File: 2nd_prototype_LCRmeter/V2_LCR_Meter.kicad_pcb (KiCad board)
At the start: 6 copper layers, 99.9 x 99.9 mm, 202 parts, among them J1 Conn_Coaxial, J2 Conn_Coaxial, J3 Conn_Coaxial, J4 Conn_Coaxial, J5 USB_C_Receptacle_USB2.0_16P, J6 IDC 2x5, J7 Display OLED, K1 Relay_DPDT, Q1 NX3008NBK, Q2 NX3008NBK, Q3 NX3008NBK, SW1 SW_SPST, SW2 SW_SPST, SW3 SW_SPST, U1 AD9837, U10 ESP32-S2-SOLO-N4, U12 TL074, U13 MCP4561-502E_MS, U14 CD74HC4052, U16 CD74HC4052, U17 INA823, U18 CD74HC4052, U19 74LVC1G02, U2 TLV9154, U20 CD74HC4052, U21 INA823, U23 CD74HC4052, U3 ADS1115IDGS, U4 LM393, U5 TLV9154, U7 TDC7200PWR, U8 LM27762, U9 HT75xx-1-SOT89, X1 SG-210STF, X2 SG-210STF

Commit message: work on layout proto2
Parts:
- removed  : TestPoint_THTPad_D2.5mm_Drill1.2mm, TestPoint:TestPoint_THTPad_D2.5mm_Drill1.2mm (x8)
- removed  : G***, kibuzzard-678FA556 (x2)
- removed  : G***, kibuzzard-678FA586 (x2)
- removed  : G***, kibuzzard-678FA580 (x2)
- removed  : G***, kibuzzard-678FA578 (x2)
- removed ? (x4): MountingHole_2.2mm_M2_DIN965_Pad, MountingHole:MountingHole_2.2mm_M2_DIN965_Pad
- removed D19, D21, D22, D23: WS2812B, LED_SMD:LED_WS2812B_PLCC4_5.0x5.0mm_P3.2mm
- removed D20: LED, LED_SMD:LED_miniPLCC_2315
- removed J5: USB_C_Receptacle_USB2.0_16P, Connector_USB:USB_C_Receptacle_GCT_USB4105-xx-A_16P_TopMnt_Horizontal
- removed Q2, Q3: NX3008NBK, Package_TO_SOT_SMD:SOT-323_SC-70_Handsoldering
- removed SW2, SW3: SW_SPST, Snapeda:SW-SMD_L6.1-W3.7-LS7.9
- removed U21: INA823, Package_SO:SOIC-8_3.9x4.9mm_P1.27mm
- removed U22: ~, Snapeda:AD9833_Module
- removed U23: CD74HC4052, Package_SO:TSSOP-16_4.4x5mm_P0.65mm
- removed X2: SG-210STF, Oscillator:Oscillator_SMD_SeikoEpson_SG210-4Pin_2.5x2.0mm
- removed kibuzzard-678FC38E: G***, kibuzzard-678FC38E
- removed kibuzzard-678FC3F7: G***, kibuzzard-678FC3F7
- removed kibuzzard-678FC3FC: G***, kibuzzard-678FC3FC
- removed kibuzzard-678FC401: G***, kibuzzard-678FC401
- removed kibuzzard-6790BC5C (x2): G***, kibuzzard-6790BC5C
- removed kibuzzard-6790BC71 (x2): G***, kibuzzard-6790BC71
- removed kibuzzard-6790BC83 (x2): G***, kibuzzard-6790BC83
- removed kibuzzard-6790BC8C (x2): G***, kibuzzard-6790BC8C
- removed kibuzzard-6790BCCF: G***, kibuzzard-6790BCCF
- removed kibuzzard-6790BCE4: G***, kibuzzard-6790BCE4
- removed kibuzzard-6790BCFE: G***, kibuzzard-6790BCFE
- removed kibuzzard-6790BDCA: G***, kibuzzard-6790BDCA
- removed kibuzzard-6790BDD8: G***, kibuzzard-6790BDD8
- removed kibuzzard-6790BDEA: G***, kibuzzard-6790BDEA
- removed kibuzzard-6790BDF0: G***, kibuzzard-6790BDF0
- removed kibuzzard-67960D2E: G***, kibuzzard-67960D2E
- removed kibuzzard-67C21963: G***, kibuzzard-67C21963
- added C24: 1u, Capacitor_SMD:C_0603_1608Metric_Pad1.08x0.95mm_HandSolder, F.Cu at (89.8, 41.0)
- added C52: 1u, Capacitor_SMD:C_0603_1608Metric_Pad1.08x0.95mm_HandSolder, F.Cu at (72.9, 91.9)
- added C53: 1u, Capacitor_SMD:C_0603_1608Metric_Pad1.08x0.95mm_HandSolder, B.Cu at (252.5, 80.8)
- added C54: 100n, Capacitor_SMD:C_0603_1608Metric_Pad1.08x0.95mm_HandSolder, B.Cu at (251.1, 76.4)
- added C55: 1u, Capacitor_SMD:C_0603_1608Metric_Pad1.08x0.95mm_HandSolder, B.Cu at (249.5, 69.7)
- added C56: 100n, Capacitor_SMD:C_0603_1608Metric_Pad1.08x0.95mm_HandSolder, B.Cu at (269.8, 84.2)
- added J8: Conn_Coaxial, Snapeda:BNC_Gold, F.Cu at (257.9, 118.5)
- added J9: Conn_Coaxial, Snapeda:BNC_Gold, F.Cu at (191.9, 118.5)
- added JP5: SolderJumper_2_Open, Jumper:SolderJumper-2_P1.3mm_Open_RoundedPad1.0x1.5mm, F.Cu at (264.4, 73.3)
- added JP6: SolderJumper_2_Open, Jumper:SolderJumper-2_P1.3mm_Open_RoundedPad1.0x1.5mm, F.Cu at (264.5, 65.6)
- added R20: 100R, Resistor_SMD:R_0603_1608Metric_Pad0.98x0.95mm_HandSolder, F.Cu at (102.8, 28.4)
- added R50: 10k, Resistor_SMD:R_0603_1608Metric_Pad0.98x0.95mm_HandSolder, F.Cu at (111.5, 38.5)
- added R51: 10k, Resistor_SMD:R_0603_1608Metric_Pad0.98x0.95mm_HandSolder, F.Cu at (111.5, 41.0)
- added R52: 10k, Resistor_SMD:R_0603_1608Metric_Pad0.98x0.95mm_HandSolder, F.Cu at (111.5, 43.5)
- added R53: 10k, Resistor_SMD:R_0603_1608Metric_Pad0.98x0.95mm_HandSolder, F.Cu at (111.5, 46.0)
- added R54: 10k, Resistor_SMD:R_0603_1608Metric_Pad0.98x0.95mm_HandSolder, F.Cu at (111.5, 48.5)
- added R55: 10k, Resistor_SMD:R_0603_1608Metric_Pad0.98x0.95mm_HandSolder, F.Cu at (111.5, 51.0)
- added R56: 10k, Resistor_SMD:R_0603_1608Metric_Pad0.98x0.95mm_HandSolder, B.Cu at (253.6, 73.3)
- added R57: 33k, Resistor_SMD:R_0603_1608Metric_Pad0.98x0.95mm_HandSolder, B.Cu at (257.0, 73.3)
- added R58: 100k, Resistor_SMD:R_0603_1608Metric_Pad0.98x0.95mm_HandSolder, B.Cu at (251.1, 73.1)
- added R59: 100k, Resistor_SMD:R_0603_1608Metric_Pad0.98x0.95mm_HandSolder, B.Cu at (251.1, 69.7)
- added R60: 10k, Resistor_SMD:R_0603_1608Metric_Pad0.98x0.95mm_HandSolder, B.Cu at (247.9, 69.7)
- added R61: 10k, Resistor_SMD:R_0603_1608Metric_Pad0.98x0.95mm_HandSolder, B.Cu at (247.9, 73.1)
- added R62: 10k, Resistor_SMD:R_0603_1608Metric_Pad0.98x0.95mm_HandSolder, B.Cu at (249.5, 73.1)
- added R63: 1k, Resistor_SMD:R_0603_1608Metric_Pad0.98x0.95mm_HandSolder, F.Cu at (205.9, 38.5)
- added R64: 10k, Resistor_SMD:R_0603_1608Metric_Pad0.98x0.95mm_HandSolder, F.Cu at (239.2, 44.8)
- added R65: 5k1, Resistor_SMD:R_0603_1608Metric_Pad0.98x0.95mm_HandSolder, F.Cu at (218.1, 30.4)
- added R66: 5k1, Resistor_SMD:R_0603_1608Metric_Pad0.98x0.95mm_HandSolder, F.Cu at (218.1, 27.0)
- added TP1: TestPoint, Connector_Pin:Pin_D1.0mm_L10.0mm, F.Cu at (80.5, 62.2)
- added TP10: TestPoint, Connector_Pin:Pin_D1.0mm_L10.0mm, F.Cu at (84.6, 78.4)
- added TP11: TestPoint, Connector_Pin:Pin_D1.0mm_L10.0mm, F.Cu at (272.0, 34.0)
- added TP12: TestPoint, Connector_Pin:Pin_D1.0mm_L10.0mm, F.Cu at (272.0, 38.0)
- added TP13: TestPoint, Connector_Pin:Pin_D1.0mm_L10.0mm, F.Cu at (272.0, 42.0)
- added TP14: TestPoint, Connector_Pin:Pin_D1.0mm_L10.0mm, F.Cu at (272.0, 46.0)
- added TP15: TestPoint, Connector_Pin:Pin_D1.0mm_L10.0mm, F.Cu at (229.0, 68.6)
- added TP16: TestPoint, Connector_Pin:Pin_D1.0mm_L10.0mm, F.Cu at (229.0, 72.7)
- added TP17: TestPoint, Connector_Pin:Pin_D1.0mm_L10.0mm, F.Cu at (229.0, 76.7)
- added TP18: TestPoint, Connector_Pin:Pin_D1.0mm_L10.0mm, F.Cu at (229.0, 80.8)
- added TP19: TestPoint, Connector_Pin:Pin_D1.0mm_L10.0mm, F.Cu at (229.0, 84.8)
- added TP2: TestPoint, Connector_Pin:Pin_D1.0mm_L10.0mm, F.Cu at (80.5, 66.2)
- added TP20: TestPoint, Connector_Pin:Pin_D1.0mm_L10.0mm, F.Cu at (270.1, 90.8)
- added TP21: TestPoint, Connector_Pin:Pin_D1.0mm_L10.0mm, F.Cu at (268.8, 104.1)
- added TP3: TestPoint, Connector_Pin:Pin_D1.0mm_L10.0mm, F.Cu at (80.5, 70.3)
- added TP4: TestPoint, Connector_Pin:Pin_D1.0mm_L10.0mm, F.Cu at (80.5, 74.3)
- added TP5: TestPoint, Connector_Pin:Pin_D1.0mm_L10.0mm, F.Cu at (80.5, 78.4)
- added TP6: TestPoint, Connector_Pin:Pin_D1.0mm_L10.0mm, F.Cu at (84.6, 62.2)
- added TP7: TestPoint, Connector_Pin:Pin_D1.0mm_L10.0mm, F.Cu at (84.6, 66.2)
- added TP8: TestPoint, Connector_Pin:Pin_D1.0mm_L10.0mm, F.Cu at (84.6, 70.3)
- added TP9: TestPoint, Connector_Pin:Pin_D1.0mm_L10.0mm, F.Cu at (84.6, 74.3)
- added U11: CD74HC4052, Package_SO:TSSOP-16_4.4x5mm_P0.65mm, F.Cu at (83.3, 43.7)
- added U15: REF3033, Package_TO_SOT_SMD:SOT-23, F.Cu at (116.2, 38.2)
- added U6: INA823, Package_SO:SOIC-8_3.9x4.9mm_P1.27mm, F.Cu at (91.8, 69.8)
- added Y1: 8MHz, Crystal:Crystal_HC49-U_Vertical, F.Cu at (182.5, 40.6)
- added kibuzzard-699D9FD2: G***, kibuzzard-699D9FD2, F.Cu at (236.0, 40.0)
- added kibuzzard-699DA048: G***, kibuzzard-699DA048, F.Cu at (267.0, 34.0)
- added kibuzzard-699DA05C: G***, kibuzzard-699DA05C, F.Cu at (267.0, 38.0)
- added kibuzzard-699DA06A: G***, kibuzzard-699DA06A, F.Cu at (224.0, 72.6)
- added kibuzzard-699DA06A: G***, kibuzzard-699DA06A, F.Cu at (267.0, 42.0)
- added kibuzzard-699DA06A: G***, kibuzzard-699DA06A, F.Cu at (224.0, 68.6)
- added kibuzzard-699DA06A: G***, kibuzzard-699DA06A, F.Cu at (224.0, 76.6)
- added kibuzzard-699DA06A: G***, kibuzzard-699DA06A, F.Cu at (224.0, 84.6)
- added kibuzzard-699DA06A: G***, kibuzzard-699DA06A, F.Cu at (224.0, 80.6)
- added kibuzzard-699DA06F: G***, kibuzzard-699DA06F, F.Cu at (267.0, 46.0)
- added kibuzzard-699DB946: G***, kibuzzard-699DB946, F.Cu at (266.2, 91.7)
- C1, C2: value 4.7u -> 20p; footprint Capacitor_SMD:C_0805_2012Metric_Pad1.18x1.45mm_HandSolder -> Capacitor_SMD:C_0603_1608Metric_Pad1.08x0.95mm_HandSolder; moved to F.Cu
- C10: footprint Capacitor_SMD:C_0603_1608Metric_Pad1.08x0.95mm_HandSolder -> Resistor_SMD:R_0603_1608Metric_Pad0.98x0.95mm_HandSolder; moved to F.Cu
- C11, C12: value 470u -> 100n; footprint Capacitor_THT:CP_Radial_D8.0mm_P3.80mm -> Capacitor_SMD:C_0603_1608Metric_Pad1.08x0.95mm_HandSolder
- C13, C15: value 1u -> 4.7u; footprint Capacitor_SMD:C_0603_1608Metric_Pad1.08x0.95mm_HandSolder -> Capacitor_SMD:C_0603_1608Metric; moved to F.Cu
- C14, C19, C4, C5: value 100n -> 1u; moved to F.Cu
- C16: value 10n -> 4.7u; footprint Capacitor_SMD:C_0603_1608Metric_Pad1.08x0.95mm_HandSolder -> Capacitor_SMD:C_0603_1608Metric; moved to F.Cu
- C17: value 1u -> 10n
- C18, C7: value 1u -> 470u; footprint Capacitor_SMD:C_0603_1608Metric_Pad1.08x0.95mm_HandSolder -> Capacitor_THT:CP_Radial_D8.0mm_P3.80mm; moved to F.Cu
- C20, C21, C22, C23, C25, C26, C27, C29, C30, C31, C35, C36, C37, C38, C41, C43, C47, C49, R15, R18, R2, R35, R5, R6, R8: moved to F.Cu
- C28, C32, C33, C34, C44, C45, C46: value 1u -> 330n; moved to F.Cu
- C3: footprint Resistor_SMD:R_0603_1608Metric_Pad0.98x0.95mm_HandSolder -> Capacitor_SMD:C_0603_1608Metric_Pad1.08x0.95mm_HandSolder; moved to F.Cu
- C39, C40, C42: value 330n -> 1u; moved to F.Cu
- C48, C50: value 1u -> 100n; moved to F.Cu
- C51: value 470u -> 1u; footprint Capacitor_THT:CP_Radial_D8.0mm_P3.80mm -> Capacitor_SMD:C_0603_1608Metric_Pad1.08x0.95mm_HandSolder
- C6: value 4.7u -> 1u; footprint Capacitor_SMD:C_0805_2012Metric_Pad1.18x1.45mm_HandSolder -> Capacitor_SMD:C_0603_1608Metric_Pad1.08x0.95mm_HandSolder; moved to F.Cu
- C8, C9: footprint Capacitor_SMD:C_0805_2012Metric_Pad1.18x1.45mm_HandSolder -> Capacitor_SMD:C_0603_1608Metric; moved to F.Cu
- D14: value LED -> D_Schottky; footprint LED_SMD:LED_miniPLCC_2315 -> Diode_SMD:D_MiniMELF
- D15, D17: value LED -> WS2812B; footprint LED_SMD:LED_miniPLCC_2315 -> LED_SMD:LED_WS2812B_PLCC4_5.0x5.0mm_P3.2mm
- D18: footprint LED_SMD:LED_miniPLCC_2315 -> LED_SMD:LED_miniPLCC_2315_Handsoldering
- D2: value D_Schottky -> LED; footprint Diode_SMD:D_MiniMELF -> LED_SMD:LED_miniPLCC_2315
- D3, D4, D5, D6: value SS14 -> LED; footprint Diode_SMD:D_SMA -> LED_SMD:LED_miniPLCC_2315
- J1: value Conn_Coaxial -> ST-Link; footprint Connector_Coaxial:BNC_Amphenol_B6252HB-NPP3G-50_Horizontal -> Connector_PinHeader_2.54mm:PinHeader_1x04_P2.54mm_Vertical_SMD_Pin1Left
- J2: value Conn_Coaxial -> Display OLED; footprint Connector_Coaxial:BNC_Amphenol_B6252HB-NPP3G-50_Horizontal -> Connector:FanPinHeader_1x04_P2.54mm_Vertical
- J3: value Conn_Coaxial -> IDC 2x5; footprint Connector_Coaxial:BNC_Amphenol_B6252HB-NPP3G-50_Horizontal -> Connector_IDC:IDC-Header_2x05_P2.54mm_Vertical
- J4: value Conn_Coaxial -> USB_C_Receptacle_USB2.0_16P; footprint Connector_Coaxial:BNC_Amphenol_B6252HB-NPP3G-50_Horizontal -> Connector_USB:USB_C_Receptacle_GCT_USB4105-xx-A_16P_TopMnt_Horizontal
- J6: value IDC 2x5 -> Conn_Coaxial; footprint Connector_IDC:IDC-Header_2x05_P2.54mm_Vertical -> Snapeda:BNC_Gold
- J7: value Display OLED -> Conn_Coaxial; footprint Connector:FanPinHeader_1x04_P2.54mm_Vertical -> Snapeda:BNC_Gold
- JP1: value SolderJumper_3_Open -> Jumper_3_Open; footprint Jumper:SolderJumper-3_P1.3mm_Open_RoundedPad1.0x1.5mm -> Connector_PinHeader_2.54mm:PinHeader_1x03_P2.54mm_Vertical_SMD_Pin1Left
- JP4: footprint Jumper:SolderJumper-2_P1.3mm_Open_TrianglePad1.0x1.5mm -> Jumper:SolderJumper-2_P1.3mm_Open_RoundedPad1.0x1.5mm
- K1: footprint Relay_THT:Relay_CIT-J104D -> Relay_THT:Relay_DPDT_Finder_30.22
- R1, R19, R22, R42, R45, R46, R47, R48, R49: value 1k -> 10k; moved to F.Cu
- R10: value 10k -> 1k5; moved to F.Cu
- R11: value 33k -> 1k5; moved to F.Cu
- R12: value 10k -> 4k7; moved to F.Cu
- R13, R37, R38: value 10k -> 1k; moved to F.Cu
- R14: value 10k -> 200k; moved to F.Cu
- R16: value 100R -> 22k; moved to F.Cu
- R17, R24, R27: value 100k -> 10k; moved to F.Cu
- R21: value 100R -> 1k; moved to F.Cu
- R23, R36: value 10k -> 100k; moved to F.Cu
- R25, R29, R30, R31: value 0R -> 10k; moved to F.Cu
- R26, R32: value 200k -> 10k; moved to F.Cu
- R28: value 22k -> 10k; moved to F.Cu
- R3, R4: value 1k5 -> 10k; moved to F.Cu
- R33: value 100k -> 100R; moved to F.Cu
- R34: value 22k -> 1k; moved to F.Cu
- R39: value 100k -> 200k; moved to F.Cu
- R40: value 1k -> 100k; moved to F.Cu
- R41: value 100k -> 22k; moved to F.Cu
- R43, R44: value 4k7 -> 10k; moved to F.Cu
- R7: value 1k -> 1k5; moved to F.Cu
- R9: value 100k -> 4k7; moved to F.Cu
- U1: value AD9837 -> STM32F103C8Tx; footprint Snapeda:AD9837_AD9837 -> Package_QFP:LQFP-48_7x7mm_P0.5mm
- U10: value ESP32-S2-SOLO-N4 -> TL072; footprint Snapeda:ESP32-S2-SOLO-N4_XCVR_ESP32-S2-SOLO-N4 -> Package_SO:SOIC-8_3.9x4.9mm_P1.27mm
- U12: value TL074 -> INA823; footprint Package_SO:TSSOP-14_4.4x5mm_P0.65mm -> Package_SO:SOIC-8_3.9x4.9mm_P1.27mm
- U13: value MCP4561-502E_MS -> CD74HC4052; footprint Snapeda:MCP4561-502E_MS_SOP65P490X110-8N -> Package_SO:TSSOP-16_4.4x5mm_P0.65mm
- U16: value CD74HC4052 -> 74LVC1G02; footprint Package_SO:TSSOP-16_4.4x5mm_P0.65mm -> Package_TO_SOT_SMD:SOT-23-5_HandSoldering
- U17: value INA823 -> ~; footprint Package_SO:SOIC-8_3.9x4.9mm_P1.27mm -> Snapeda:AD9833_Module
- U18: value CD74HC4052 -> TL074; footprint Package_SO:TSSOP-16_4.4x5mm_P0.65mm -> Package_SO:TSSOP-14_4.4x5mm_P0.65mm
- U19: value 74LVC1G02 -> MCP4561-502E_MS; footprint Package_TO_SOT_SMD:SOT-23-5_HandSoldering -> Package_SO:MSOP-8_3x3mm_P0.65mm
- U2: value TLV9154 -> LM27762; footprint Package_SO:SOIC-14_3.9x8.7mm_P1.27mm -> Package_SON:WSON-12-1EP_3x2mm_P0.5mm_EP1x2.65_ThermalVias
- U20: value CD74HC4052 -> AD9837; footprint Package_SO:TSSOP-16_4.4x5mm_P0.65mm -> Package_CSP:LFCSP-WD-10-1EP_3x3mm_P0.5mm_EP1.64x2.38mm
- U3: value ADS1115IDGS -> HT75xx-1-SOT89; footprint Package_SO:TSSOP-10_3x3mm_P0.5mm -> Package_TO_SOT_SMD:SOT-89-3_Handsoldering
- U4: value LM393 -> OPA2192
- U5: value TLV9154 -> CD74HC4052; footprint Package_SO:SOIC-14_3.9x8.7mm_P1.27mm -> Package_SO:TSSOP-16_4.4x5mm_P0.65mm
- U7: value TDC7200PWR -> TL074; footprint Snapeda:TDC7200PWR_SOP65P640X120-14N -> Package_SO:TSSOP-14_4.4x5mm_P0.65mm
- U8: value LM27762 -> CD74HC4052; footprint Package_SON:WSON-12-1EP_3x2mm_P0.5mm_EP1x2.65_ThermalVias -> Package_SO:TSSOP-16_4.4x5mm_P0.65mm
- U9: value HT75xx-1-SOT89 -> TL074; footprint Package_TO_SOT_SMD:SOT-89-3_Handsoldering -> Package_SO:TSSOP-14_4.4x5mm_P0.65mm
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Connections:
- C1 pad 1: +5V_USB -> Net-(U1-PD0)
- C10 pad 1: GND -> Net-(U2-C+)
- C10 pad 2: +3V3 -> Net-(U2-C-)
- C12 pad 1: -5V -> +3V3
- C13 pad 1: GND -> Net-(U2-CP)
- C13 pad 2: +3V3 -> GND
- C14 pad 1: GND -> +3V3
- C14 pad 2: Net-(U1-CAP/2.5V) -> GND
- C15 pad 1: GND -> +5V_USB
- C15 pad 2: Net-(U1-CAP/2.5V) -> GND
- C16 pad 1: Net-(U1-COMP) -> +5V
- C16 pad 2: +3V3 -> GND
- C17 pad 1: GND -> +3V3
- C17 pad 2: +5V -> Net-(U20-COMP)
- C18 pad 1: GND -> -5V
- C18 pad 2: -5V -> GND
- C19 pad 1: Net-(U12B-+) -> GND
- C19 pad 2: Net-(U13-P0W) -> +5V
- C2 pad 1: +5V_USB -> Net-(U1-PD1)
- C20 pad 2: +3V3 -> -5V
- C21 pad 2: Net-(U12D-+) -> -5V
- C23 pad 2: +5V -> -5V
- C27 pad 2: +5V -> -5V
- C28 pad 1: GND -> Net-(C28-Pad1)
- C28 pad 2: -5V -> Net-(C28-Pad2)
- C3 pad 1: Net-(U8-C+) -> GND
- C3 pad 2: Net-(U8-C-) -> +3V3
- C32 pad 1: GND -> Net-(U7C-+)
- C32 pad 2: -5V -> Net-(C28-Pad1)
- C33 pad 1: GND -> Net-(U7A-+)
- C33 pad 2: -5V -> GND
- C34 pad 1: GND -> /Analog frontend/V_LowPass
- C34 pad 2: -5V -> Net-(C34-Pad2)
- C35 pad 2: -5V -> +5V
- C36 pad 2: +5V -> -5V
- C37 pad 2: +5V -> -5V
- C38 pad 2: -5V -> +5V
- C39 pad 1: V_Mean -> GND
- C39 pad 2: Net-(C39-Pad2) -> -5V
- C4 pad 1: +5V_USB -> GND
- C4 pad 2: GND -> +3V3
- C40 pad 1: Net-(U5A-+) -> GND
- C40 pad 2: GND -> +5V
- C41 pad 2: V_Peak -> -5V
- C42 pad 1: Net-(U5C-+) -> GND
- C42 pad 2: GND -> +5V
- C43 pad 1: I_Mean -> Net-(C43-Pad1)
- C44 pad 1: GND -> Net-(U9C-+)
- C44 pad 2: I_Peak -> Net-(C43-Pad1)
- C45 pad 1: GND -> Net-(U9A-+)
- C45 pad 2: +3V3 -> GND
- C46 pad 1: GND -> /Analog frontend/I_LowPass
- C46 pad 2: +5V -> Net-(C46-Pad2)
- C47 pad 1: Net-(D6-K) -> GND
- C47 pad 2: Net-(U5D-+) -> +5V
- C48 pad 2: +3V3 -> +3.3 V_{ref}
- C49 pad 1: Net-(D5-K) -> GND
- C49 pad 2: Net-(U5B-+) -> Net-(U10A-+)
- C5 pad 1: +3V3 -> GND
- C5 pad 2: GND -> +3V3
- C50 pad 1: Net-(U7-VREG) -> GND
- C50 pad 2: GND -> +1.65 V_{ref}
- C51 pad 1: +5V -> GND
- C51 pad 2: GND -> +5V
- C6 pad 1: Net-(U8-CP) -> GND
- C6 pad 2: GND -> +3V3
- C7 pad 1: +3V3 -> +5V_USB
- C8 pad 1: -5V -> +5V_USB
- C9 pad 1: +5V -> -5V
- D14 pad 1: GND -> +5V
- D15 pad 1: GND -> +5V_USB
- D15 pad 2: Net-(D15-A) -> unconnected-(D15-DOUT-Pad2)
- D16 pad 1: GND -> Net-(D16-K)
- D16 pad 2: Net-(D16-A) -> /LEDs/LED_1
- D17 pad 1: GND -> +5V_USB
- D17 pad 2: Net-(D17-A) -> Net-(D15-DIN)
- D18 pad 1: GND -> Net-(D18-K)
- D18 pad 2: Net-(D18-A) -> +5V_USB
- D2 pad 1: +5V -> GND
- D3 pad 1: V_Peak -> GND
- D4 pad 1: I_Peak -> GND
- D5 pad 1: Net-(D5-K) -> GND
- D5 pad 2: GND -> Net-(D5-A)
- D6 pad 1: Net-(D6-K) -> GND
- D6 pad 2: GND -> Net-(D6-A)
- J1 pad 1: SW_BYPASS_2_A -> +3V3
- J1 pad 2: BNC_Shield -> SWDIO
- J2 pad 1: Net-(J2-In) -> +3V3
- J2 pad 2: BNC_Shield -> GND
- J3 pad 1: Net-(J3-In) -> +3V3
- J3 pad 2: BNC_Shield -> GND
- J6 pad 1: +3V3 -> Net-(J6-In)
- J6 pad 2: Net-(J6-Pin_2) -> GND
- J7 pad 1: +3V3 -> Net-(J7-In)
- JP1 pad 1: GND -> Net-(JP1-A)
- JP1 pad 3: +3V3 -> Net-(JP1-B)
- JP2 pad 1: Net-(JP2-A) -> GND
- JP2 pad 2: unconnected-(JP2-C-Pad2) -> Net-(JP2-C)
- JP2 pad 3: Net-(JP2-B) -> +3V3
- JP3 pad 1: Net-(JP3-A) -> /Drive signal source/S_Clock
- JP3 pad 2: /Drive signal source/S_Clock -> Net-(JP3-B)
- JP4 pad 1: GND -> Net-(JP4-A)
- JP4 pad 2: BNC_Shield -> Net-(JP4-B)
- K1 pad A2: Net-(D2-A) -> Net-(D14-A)
- Q1 pad 3: Net-(D2-A) -> Net-(D14-A)
- R1 pad 1: Net-(D1-A) -> GND
- R1 pad 2: +5V_USB -> Net-(JP1-A)
- R10 pad 1: Net-(R10-Pad1) -> Net-(U2-FB+)
- R11 pad 1: Net-(U12A--) -> Net-(U2-FB-)
- R11 pad 2: Net-(R10-Pad1) -> GND
- R12 pad 1: Net-(U12B--) -> Net-(U2-FB-)
- R12 pad 2: Net-(U12C--) -> -5V
- R13 pad 1: Net-(U12D--) -> +3V3
- R13 pad 2: Net-(U12C--) -> Net-(U5-Y)
- R14 pad 1: Net-(U12C--) -> Net-(U5-X1)
- R14 pad 2: /Analog frontend/Sig_IN -> Rg_1_B
- R15 pad 1: /Drive signal source/Offset_PWM -> unconnected-(R15-Pad1)
- R15 pad 2: Net-(U12D-+) -> Rg_1_B
- R16 pad 1: SW_BYPASS_1_B -> Net-(U5-X3)
- R16 pad 2: Net-(J4-In) -> Rg_1_B
- R17 pad 1: Net-(U14-X3) -> Net-(C28-Pad2)
- R17 pad 2: Net-(J4-In) -> Net-(C34-Pad2)
- R18 pad 1: Net-(U14-X2) -> Net-(C34-Pad2)
- R18 pad 2: Net-(J4-In) -> Net-(U7A-+)
- R19 pad 1: Net-(U14-X1) -> Net-(U7C-+)
- R19 pad 2: Net-(J4-In) -> GND
- R2 pad 1: Net-(U8-FB+) -> +3V3
- R2 pad 2: +5V -> I2C_SDA
- R21 pad 1: SW_BYPASS_2_B -> Net-(U8-X1)
- R21 pad 2: I_Sens -> Net-(J8-In)
- R22 pad 1: Net-(U16-X1) -> Net-(U8-X2)
- R22 pad 2: I_Sens -> Net-(J8-In)
- R23 pad 1: Net-(U16-X2) -> Net-(U8-X3)
- R23 pad 2: I_Sens -> Net-(J8-In)
- R24 pad 1: Net-(U16-X3) -> Net-(C28-Pad1)
- R24 pad 2: I_Sens -> /Analog frontend/V_HighPass
- R25 pad 1: Net-(U18-X1) -> Net-(U7B-+)
- R25 pad 2: Net-(R25-Pad2) -> +1.65 V_{ref}
- R26 pad 1: Net-(R25-Pad2) -> Net-(U7B-+)
- R26 pad 2: Rg_1_B -> /Analog frontend/V_LowPass
- R27 pad 1: Net-(U18-X2) -> Net-(U7D-+)
- R27 pad 2: Rg_1_B -> +1.65 V_{ref}
- R28 pad 1: Net-(R28-Pad1) -> Net-(U7D-+)
- R28 pad 2: Rg_1_B -> /Analog frontend/V_HighPass
- R29 pad 1: Net-(U18-X3) -> Net-(U7B--)
- R29 pad 2: Net-(R28-Pad1) -> GND
- R3 pad 1: Net-(U8-FB+) -> Net-(JP1-B)
- R3 pad 2: GND -> +3V3
- R30 pad 1: Net-(U20-X1) -> Net-(U7D--)
- R30 pad 2: Net-(R30-Pad2) -> GND
- R31 pad 1: Net-(U20-X3) -> Net-(U7B--)
- R31 pad 2: Net-(R31-Pad2) -> /Analog frontend/V_ADC_DC
- R32 pad 1: Net-(R30-Pad2) -> Net-(U7D--)
- R32 pad 2: Rg_2_B -> /Analog frontend/V_ADC_AC
- R33 pad 1: Net-(U20-X2) -> SW_BYPASS_2_B
- R33 pad 2: Rg_2_B -> Net-(U12-+)
- R34 pad 1: Net-(R31-Pad2) -> Net-(U11-X1)
- R34 pad 2: Rg_2_B -> Net-(U12-+)
- R35 pad 1: Net-(C39-Pad2) -> Net-(U11-X2)
- R35 pad 2: Net-(U5A-+) -> Net-(U12-+)
- R36 pad 1: Net-(U5B-+) -> Net-(U11-X3)
- R36 pad 2: Net-(C39-Pad2) -> Net-(U12-+)
- R37 pad 1: Net-(U5D-+) -> +3V3
- R37 pad 2: Net-(C43-Pad2) -> Net-(U13-Y)
- R38 pad 1: Net-(C43-Pad2) -> +3V3
- R38 pad 2: Net-(U5C-+) -> Net-(U14-X)
- R39 pad 1: Net-(D5-K) -> Net-(U13-X1)
- R39 pad 2: GND -> Rg_2_B
- R4 pad 1: Net-(U8-FB-) -> GND
- R4 pad 2: GND -> Net-(U1-PB2)
- R40 pad 1: +3V3 -> Net-(U13-X2)
- R40 pad 2: V_Square -> Rg_2_B
- R41 pad 1: Net-(D6-K) -> Net-(U13-X3)
- R41 pad 2: GND -> Rg_2_B
- R42 pad 1: +3V3 -> Net-(C43-Pad2)
- R42 pad 2: I_Square -> Net-(C46-Pad2)
- R43 pad 1: +3V3 -> Net-(C46-Pad2)
- R43 pad 2: I2C_SDA -> Net-(U9A-+)
- R44 pad 1: +3V3 -> Net-(U9C-+)
- R44 pad 2: I2C_SCL -> GND
- R45 pad 1: +3V3 -> Net-(C43-Pad1)
- R45 pad 2: Net-(U23-X) -> /Analog frontend/I_HighPass
- R46 pad 1: +3V3 -> Net-(U9B-+)
- R46 pad 2: Net-(U18-Y) -> +1.65 V_{ref}
- R47 pad 1: +3V3 -> Net-(U9B-+)
- R47 pad 2: Net-(U20-Y) -> /Analog frontend/I_LowPass
- R48 pad 1: GND -> Net-(U9D-+)
- R48 pad 2: Net-(D20-K) -> +1.65 V_{ref}
- R49 pad 1: +3V3 -> Net-(U9D-+)
- R49 pad 2: Net-(SW3-B) -> /Analog frontend/I_HighPass
- R5 pad 1: Net-(U8-FB-) -> +3V3
- R5 pad 2: -5V -> I2C_SCL
- R7 pad 1: GND -> +3V3
- R7 pad 2: Net-(U10-IO46) -> /Power supply + USB/USB_D+
- R8 pad 1: +3V3 -> Net-(D1-A)
- R8 pad 2: Net-(SW2-B) -> +5V_USB
- R9 pad 1: Net-(U12B-+) -> Net-(U2-FB+)
- R9 pad 2: GND -> +5V
- U10 pad 1: GND -> +1.65 V_{ref}
- U10 pad 2: +3V3 -> +1.65 V_{ref}
- U10 pad 3: Net-(SW1-B) -> Net-(U10A-+)
- U10 pad 4: /Drive signal source/Offset_PWM -> -5V
- U10 pad 5: TDC_Int -> unconnected-(U10B-+-Pad5)
- U10 pad 6: TDC_Trig -> unconnected-(U10B---Pad6)
- U10 pad 7: /LEDs/RGB_Data -> unconnected-(U10-Pad7)
- U10 pad 8: Net-(SW3-B) -> +5V
- U12 pad 1: unconnected-(U12-Pad1) -> Rg_2_B
- U12 pad 2: Net-(U12A--) -> Net-(U11-Y)
- U12 pad 3: unconnected-(U12A-+-Pad3) -> Net-(U12-+)
- U12 pad 4: +5V -> -5V
- U12 pad 5: Net-(U12B-+) -> GND
- U12 pad 6: Net-(U12B--) -> Net-(C43-Pad2)
- U12 pad 7: Net-(U12B--) -> +5V
- U12 pad 8: /Analog frontend/Sig_IN -> Rg_2_A
- U13 pad 1: Net-(JP1-C) -> Net-(D6-A)
- U13 pad 2: I2C_SCL -> Net-(D8-A)
- U13 pad 3: I2C_SDA -> Net-(U13-Y)
- U13 pad 4: GND -> Net-(D9-A)
- U13 pad 5: Net-(U12A--) -> Net-(D7-A)
- U13 pad 6: Net-(U13-P0W) -> GND
- U13 pad 7: GND -> -5V
- U13 pad 8: +3V3 -> GND
- U14 pad 1: SW_BYPASS_1_B -> unconnected-(U14-Y0-Pad1)
- U14 pad 10: I_Range_A -> Shunt_Range_A
- U14 pad 11: Net-(U14-X3) -> Net-(D13-A)
- U14 pad 12: SW_BYPASS_1_B -> Net-(D10-A)
- U14 pad 13: SW_BYPASS_1_A -> Net-(U14-X)
- U14 pad 14: Net-(U14-X1) -> Net-(D11-A)
- U14 pad 15: Net-(U14-X2) -> Net-(D12-A)
- U14 pad 16: +5V -> +3V3
- U14 pad 2: Net-(U14-X2) -> unconnected-(U14-Y2-Pad2)
- U14 pad 3: Net-(U14-Y) -> unconnected-(U14-Y-Pad3)
- U14 pad 4: Net-(U14-X3) -> unconnected-(U14-Y3-Pad4)
- U14 pad 5: Net-(U14-X1) -> unconnected-(U14-Y1-Pad5)
- U14 pad 7: -5V -> GND
- U14 pad 9: I_Range_B -> Shunt_Range_B
- U16 pad 1: SW_BYPASS_2_B -> Shunt_Range_A
- U16 pad 2: Net-(U16-X2) -> Shunt_Range_B
- U16 pad 3: Net-(U16-Y) -> GND
- U16 pad 4: Net-(U16-X3) -> Net-(Q1-G)
- U16 pad 5: Net-(U16-X1) -> +5V
- U17 pad 1: Rg_1_B -> +3V3
- U17 pad 2: Net-(J2-In) -> GND
- U17 pad 3: Net-(J3-In) -> /Drive signal source/S_Data
- U17 pad 4: -5V -> Net-(JP6-A)
- U17 pad 5: GND -> /Drive signal source/F_Sync
- U17 pad 6: Net-(U5B-+) -> GND
- U17 pad 7: +5V -> Net-(JP5-A)
- U18 pad 1: Net-(D15-A) -> Net-(U19-P0A)
- U18 pad 10: V_PGA_A -> Net-(U18C-+)
- U18 pad 11: Net-(U18-X3) -> -5V
- U18 pad 12: unconnected-(U18-X0-Pad12) -> Net-(U18D-+)
- U18 pad 13: Rg_1_A -> GND
- U18 pad 14: Net-(U18-X1) -> /Analog frontend/Sig_IN
- U18 pad 2: Net-(D17-A) -> Net-(U18A--)
- U18 pad 3: Net-(U18-Y) -> Net-(JP4-B)
- U18 pad 4: Net-(D18-A) -> +5V
- U18 pad 5: Net-(D16-A) -> Net-(U18B-+)
- U18 pad 6: GND -> Net-(U18B--)
- U18 pad 7: -5V -> Net-(U18B--)
- U18 pad 8: GND -> Net-(U18C--)
- U18 pad 9: V_PGA_B -> Net-(U18C--)
- U19 pad 1: I_Range_A -> Net-(JP2-C)
- U19 pad 2: I_Range_B -> I2C_SCL
- U19 pad 3: GND -> I2C_SDA
- U19 pad 4: Net-(Q1-G) -> GND
- U19 pad 5: +5V -> Net-(U19-P0A)
- U2 pad 1: SW_BYPASS_1_A -> Net-(D18-K)
- U2 pad 10: Net-(U2C-+) -> Net-(U2-C+)
- U2 pad 11: -5V -> +5V
- U2 pad 12: Net-(U2D-+) -> +5V_USB
- U2 pad 13: Net-(U2D-+) -> GND
- U2 pad 2: Net-(U14-Y) -> Net-(U2-FB+)
- U2 pad 3: /Analog frontend/Sig_IN -> +5V_USB
- U2 pad 4: +5V -> GND
- U2 pad 5: GND -> Net-(U2-CP)
- U2 pad 6: Net-(U16-Y) -> -5V
- U2 pad 7: I_Sens -> Net-(U2-FB-)
- U2 pad 8: Net-(U2C-+) -> +5V_USB
- U2 pad 9: Net-(U2C-+) -> Net-(U2-C-)
- U20 pad 1: Net-(D11-A) -> Net-(U20-COMP)
- U20 pad 10: I_PGA_A -> Net-(JP4-A)
- U20 pad 2: Net-(D13-A) -> +3V3
- U20 pad 3: Net-(U20-Y) -> Net-(U20-CAP/2.5V)
- U20 pad 4: Net-(D14-A) -> GND
- U20 pad 5: Net-(D12-A) -> Net-(U20-MCLK)
- U20 pad 6: GND -> /Drive signal source/S_Data
- U20 pad 7: -5V -> Net-(JP3-B)
- U20 pad 8: GND -> /Drive signal source/F_Sync
- U20 pad 9: I_PGA_B -> GND
- U3 pad 2: ADC_Alert -> +5V_USB
- U3 pad 3: GND -> +3V3
- U4 pad 1: V_Square -> SW_BYPASS_1_A
- U4 pad 2: GND -> Net-(U4A--)
- U4 pad 3: Net-(D5-K) -> /Analog frontend/Sig_IN
- U4 pad 4: GND -> -5V
- U4 pad 5: Net-(D6-K) -> Net-(U11-Y)
- U4 pad 7: I_Square -> Net-(U12-+)
- U5 pad 1: V_Mean -> Net-(D2-A)
- U5 pad 10: Net-(U5C-+) -> V_PGA_A
- U5 pad 11: -5V -> Net-(U5-X3)
- U5 pad 12: Net-(U5D-+) -> unconnected-(U5-X0-Pad12)
- U5 pad 13: I_Peak -> Rg_1_A
- U5 pad 14: Net-(D4-A) -> Net-(U5-X1)
- U5 pad 2: V_Mean -> Net-(D4-A)
- U5 pad 3: Net-(U5A-+) -> Net-(U5-Y)
- U5 pad 4: +5V -> Net-(D5-A)
- U5 pad 5: Net-(U5B-+) -> Net-(D3-A)
- U5 pad 6: V_Peak -> GND
- U5 pad 7: Net-(D3-A) -> -5V
- U5 pad 8: I_Mean -> GND
- U5 pad 9: I_Mean -> V_PGA_B
- U7 pad 1: TDC_Enable -> /Analog frontend/V_LowPass
- U7 pad 10: TDC_MOSI -> Net-(U7C-+)
- U7 pad 11: TDC_!CS -> -5V
- U7 pad 12: TDC_SCLK -> Net-(U7D-+)
- U7 pad 13: Net-(U7-VREG) -> Net-(U7D--)
- U7 pad 14: +3V3 -> /Analog frontend/V_ADC_AC
- U7 pad 2: TDC_Int -> /Analog frontend/V_LowPass
- U7 pad 3: V_Square -> Net-(U7A-+)
- U7 pad 4: I_Square -> +5V
- U7 pad 5: Net-(U7-CLOCK) -> Net-(U7B-+)
- U7 pad 6: unconnected-(U7-NC-Pad6) -> Net-(U7B--)
- U7 pad 7: GND -> /Analog frontend/V_ADC_DC
- U7 pad 8: TDC_Trig -> /Analog frontend/V_HighPass
- U7 pad 9: TDC_MISO -> /Analog frontend/V_HighPass
- U8 pad 1: GND -> SW_BYPASS_1_B
- U8 pad 10: Net-(U8-C+) -> Shunt_Range_A
- U8 pad 11: +5V -> Net-(U8-X3)
- U8 pad 12: +5V_USB -> SW_BYPASS_1_B
- U8 pad 13: GND -> SW_BYPASS_1_A
- U8 pad 2: Net-(U8-FB+) -> Net-(U8-X2)
- U8 pad 3: +5V_USB -> Net-(U4A--)
- U8 pad 4: GND -> Net-(U8-X3)
- U8 pad 5: Net-(U8-CP) -> Net-(U8-X1)
- U8 pad 6: -5V -> GND
- U8 pad 7: Net-(U8-FB-) -> -5V
- U8 pad 8: +5V_USB -> GND
- U8 pad 9: Net-(U8-C-) -> Shunt_Range_B
- U9 pad 1: GND -> /Analog frontend/I_LowPass
- U9 pad 2: +5V_USB -> /Analog frontend/I_LowPass
- U9 pad 3: +3V3 -> Net-(U9A-+)
- X1 pad 3: Net-(U1-MCLK) -> Net-(U20-MCLK)
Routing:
- net GND: track 228.7 -> 61.8 mm, vias 79 -> 35
- net BNC_Shield: track 162.1 -> 0.00 mm
- net I2C_SDA: track 200.1 -> 38.4 mm, vias 3 -> 1
- net I2C_SCL: track 184.6 -> 47.0 mm, vias 3 -> 1
- net I_Range_B: track 103.2 -> 0.00 mm, vias 4 -> 0
- net I_Range_A: track 101.3 -> 0.00 mm, vias 2 -> 0
- net V_Square: track 77.7 -> 0.00 mm, vias 3 -> 0
- net SW_BYPASS_2_A: track 75.2 -> 0.00 mm, vias 1 -> 0
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- added copper zone on In3.Cu, net +5V
- added copper zone on B.Cu, net +5V_USB
- added copper zone on In1.Cu, net GND
- removed copper zone on In1.Cu, net +5V
- removed copper zone on In3.Cu, net GND
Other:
- board size 99.9 x 99.9 mm -> 99.8 x 99.8 mm
- board text removed: "Addr"
- board text removed: "Chip/Module"
- board text removed: "LCR Meter Design: Vojtěch Glombíček"

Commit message: routing v2 work almost complete
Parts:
- added kibuzzard-699DC026: G***, kibuzzard-699DC026, F.Cu at (248.4, 81.0)
- added kibuzzard-69A05110: G***, kibuzzard-69A05110, F.Cu at (221.0, 105.8)
- added kibuzzard-69A0511F: G***, kibuzzard-69A0511F, F.Cu at (224.4, 105.8)
- added kibuzzard-69A0514C: G***, kibuzzard-69A0514C, F.Cu at (221.0, 85.0)
- added kibuzzard-69A05154: G***, kibuzzard-69A05154, F.Cu at (224.4, 85.0)
- added kibuzzard-69A0516F: G***, kibuzzard-69A0516F, F.Cu at (182.2, 80.3)
- added kibuzzard-69A0517C: G***, kibuzzard-69A0517C, F.Cu at (181.6, 72.5)
- C19, C20, C21, C22, C23, C24, C25, C26, C27, C28, C29, C30, C31, C32, C33, C34, C35, C36, C37, C38, C39, C40, C41, C42, C43, C44, C45, C46, C47, C48, C49, C50, C51, C52, R13, R14, R15, R16, R17, R18, R19, R20, R21, R22, R23, R24, R25, R26, R27, R28, R29, R30, R31, R32, R33, R34, R35, R36, R37, R38, R39, R40, R41, R42, R43, R44, R45, R46, R47, R48, R49, R50, R51, R52, R53, R54, R55: moved to B.Cu
- moved C51 184.1 mm to (256.1, 70.9), turned to -90 degrees
- moved C52 182.0 mm to (253.7, 70.9), turned to -90 degrees
- moved U11 178.6 mm to (254.2, 95.4), turned to 90 degrees
- moved C19 173.8 mm to (249.2, 97.8)
- moved C37 172.0 mm to (256.8, 97.0), turned to 180 degrees
- moved U8 169.2 mm to (242.1, 95.4), turned to 90 degrees
- moved C20 169.2 mm to (247.2, 93.0), turned to 180 degrees
- moved C38 166.7 mm to (253.0, 94.0), turned to 180 degrees
- moved C27 161.2 mm to (243.8, 96.2), turned to -90 degrees
- moved R33 160.9 mm to (254.8, 92.4), turned to 180 degrees
- moved U14 159.9 mm to (241.7, 78.7), turned to 90 degrees
- moved U4 159.6 mm to (248.2, 95.4), turned to -90 degrees
- moved R21 158.6 mm to (244.6, 102.0), turned to -90 degrees
- moved R36 157.5 mm to (254.8, 90.8), turned to 180 degrees
- moved R34 157.2 mm to (253.2, 89.2)
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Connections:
- D14 pad 1: +5V -> +5V_USB
- K1 pad A1: +5V -> +5V_USB
- R15 pad 1: unconnected-(R15-Pad1) -> Net-(U5-X2)
- U1 pad 11: /Analog frontend/I_ADC_DC -> /Analog frontend/V_ADC_AC
- U1 pad 13: /Analog frontend/I_ADC_AC -> /Analog frontend/I_ADC_DC
- U1 pad 14: /Analog frontend/V_ADC_AC -> /Analog frontend/I_ADC_AC
- U16 pad 5: +5V -> +5V_USB
- U5 pad 15: unconnected-(U5-X2-Pad15) -> Net-(U5-X2)
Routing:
- net SW_BYPASS_2_A: track 0.00 -> 125.1 mm, vias 0 -> 3
- net +1.65 V_{ref}: track 0.00 -> 109.6 mm, vias 0 -> 5
- net Shunt_Range_B: track 13.6 -> 111.5 mm, vias 1 -> 3
- net I2C_SDA: track 38.4 -> 135.4 mm, vias 1 -> 3
- net Shunt_Range_A: track 16.3 -> 112.3 mm, vias 1 -> 3
- net I2C_SCL: track 47.0 -> 135.6 mm, vias 1 -> 2
- net GND: track 61.8 -> 144.0 mm, vias 35 -> 76
- net /Analog frontend/I_ADC_DC: track 9.01 -> 85.2 mm
- net I_PGA_A: track 0.00 -> 73.9 mm, vias 0 -> 4
- net I_PGA_B: track 0.00 -> 70.6 mm, vias 0 -> 4
- net V_PGA_B: track 0.00 -> 68.4 mm, vias 0 -> 4
- net /Analog frontend/V_ADC_DC: track 7.98 -> 74.0 mm
- net /Analog frontend/V_ADC_AC: track 3.00 -> 66.1 mm
- net V_PGA_A: track 0.00 -> 62.5 mm, vias 0 -> 4
- net /Analog frontend/I_ADC_AC: track 3.20 -> 65.4 mm
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
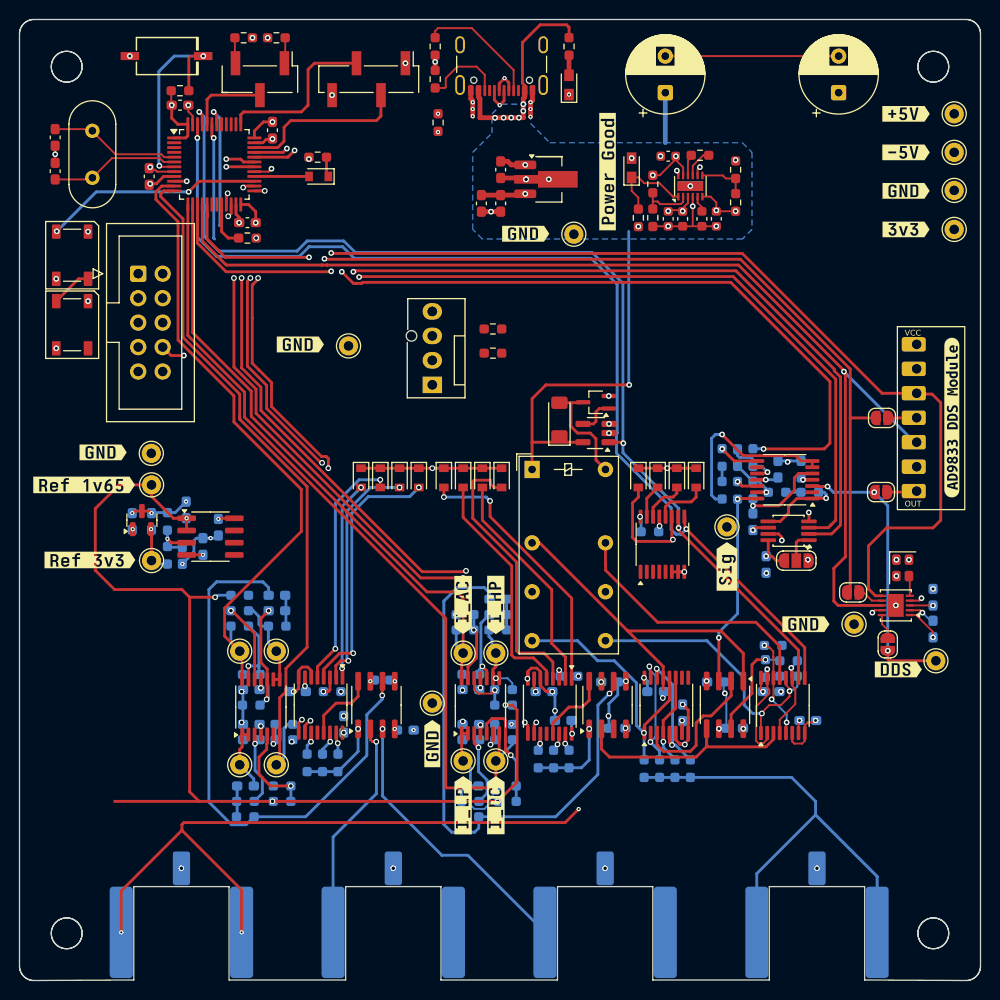
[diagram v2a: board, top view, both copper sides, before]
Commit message: finished with offset amps
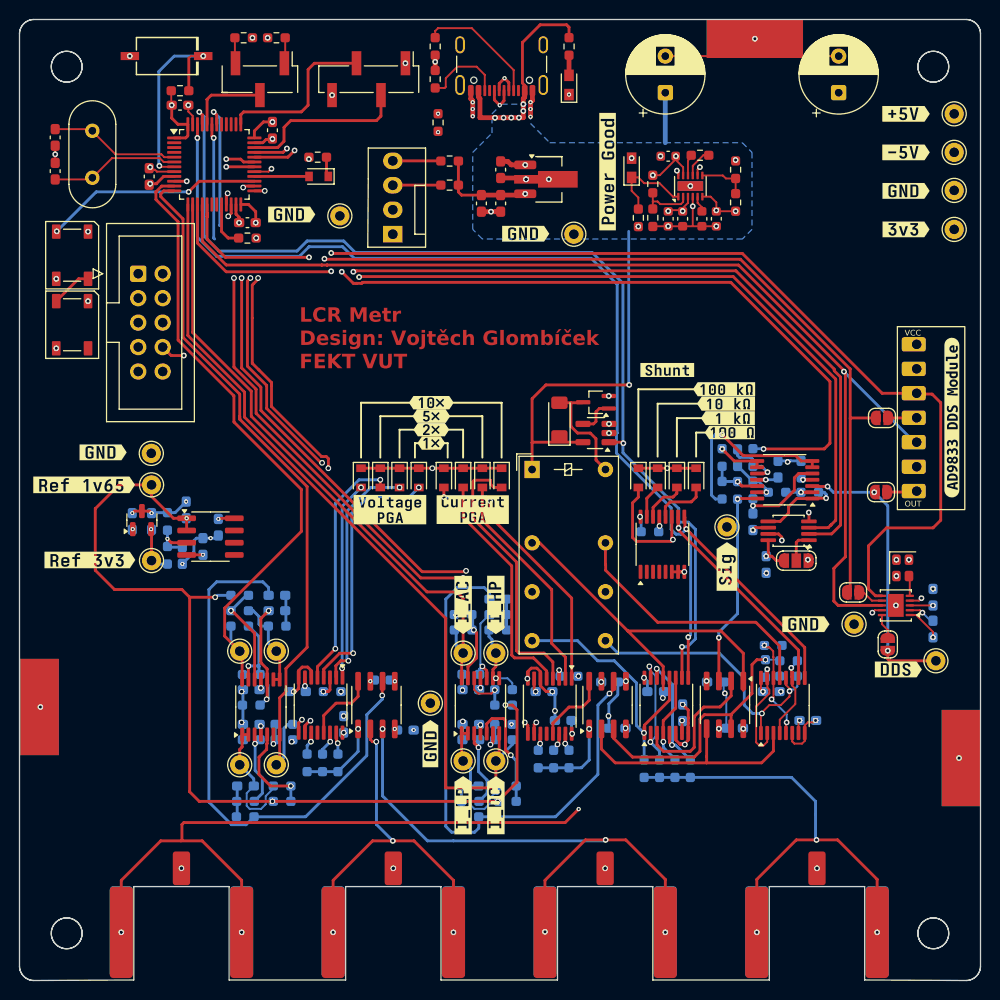
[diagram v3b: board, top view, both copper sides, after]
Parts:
- added REF**: TestPoint_Pad_4.0x4.0mm, TestPoint:TestPoint_Pad_4.0x4.0mm, F.Cu at (272.7, 100.9)
- added REF**: TestPoint_Pad_4.0x4.0mm, TestPoint:TestPoint_Pad_4.0x4.0mm, F.Cu at (251.3, 26.2)
- added REF**: TestPoint_Pad_4.0x4.0mm, TestPoint:TestPoint_Pad_4.0x4.0mm, F.Cu at (177.0, 95.6)
- added kibuzzard-69A6FBA9: G***, kibuzzard-69A6FBA9, F.Cu at (217.7, 68.2)
- added kibuzzard-69A6FBC7: G***, kibuzzard-69A6FBC7, F.Cu at (217.7, 65.4)
- added kibuzzard-69A6FBD5: G***, kibuzzard-69A6FBD5, F.Cu at (217.7, 64.0)
- added kibuzzard-69A6FBDC: G***, kibuzzard-69A6FBDC, F.Cu at (217.7, 66.8)
- added kibuzzard-69A6FC6B: G***, kibuzzard-69A6FC6B, F.Cu at (213.4, 75.1)
- added kibuzzard-69A6FC8C: G***, kibuzzard-69A6FC8C, F.Cu at (222.0, 75.1)
- added kibuzzard-69A6FD14: G***, kibuzzard-69A6FD14, F.Cu at (248.3, 64.1)
- added kibuzzard-69A6FD3E: G***, kibuzzard-69A6FD3E, F.Cu at (248.5, 65.6)
- added kibuzzard-69A6FD47: G***, kibuzzard-69A6FD47, F.Cu at (248.7, 67.1)
- added kibuzzard-69A6FD75: G***, kibuzzard-69A6FD75, F.Cu at (248.1, 62.6)
- added kibuzzard-69A6FDE1: G***, kibuzzard-69A6FDE1, F.Cu at (242.2, 60.6)
- moved R5 18.0 mm to (219.6, 41.4), turned to 180 degrees
- moved R2 18.0 mm to (219.6, 38.9), turned to 180 degrees
- moved J2 16.2 mm to (213.7, 46.5)
- moved TP18 13.5 mm to (208.2, 44.6)
- moved kibuzzard-699DA06A 13.5 mm to (203.2, 44.5)
- moved J6 0.56 mm to (213.8, 119.1)
- moved J8 0.46 mm to (257.8, 119.0)
- moved J7 0.41 mm to (235.8, 119.0)
- moved TP19 0.20 mm to (217.6, 95.2)
- moved kibuzzard-699DA06A 0.20 mm to (217.6, 99.4)
- moved R51 0.20 mm to (221.0, 86.0)
- moved R53 0.20 mm to (221.0, 87.6)
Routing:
- net Net-(J7-In): track 29.7 -> 58.9 mm, vias 1 -> 4
- net I2C_SDA: track 135.4 -> 158.7 mm
- net Shunt_Range_A: track 112.3 -> 130.6 mm, vias 3 -> 4
- net Net-(U12-+): track 13.9 -> 31.5 mm
- net I2C_SCL: track 135.6 -> 152.1 mm
- net Shunt_Range_B: track 111.5 -> 127.6 mm, vias 3 -> 4
- net Net-(J6-In): track 23.5 -> 39.5 mm, vias 1 -> 4
- net +1.65 V_{ref}: track 109.6 -> 100.7 mm
- net /Analog frontend/V_LowPass: track 6.70 -> 13.3 mm
- net +3V3: track 28.7 -> 34.4 mm
- net Net-(U7D-+): track 8.22 -> 10.5 mm
- net Net-(U18D-+): track 3.80 -> 5.39 mm
- net SW_BYPASS_2_A: track 125.1 -> 126.6 mm, vias 3 -> 5
- net Net-(U18A--): track 1.57 -> 2.75 mm, vias 0 -> 1
- net Net-(U11-Y): track 25.4 -> 26.5 mm
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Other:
- board text added: "LCR Metr Design: Vojtěch Glombíček FEKT VUT"

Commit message: finished final final_2
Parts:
- removed C29, C30: 1u, Capacitor_SMD:C_0603_1608Metric_Pad1.08x0.95mm_HandSolder
- removed R25, R26, R27, R28, R29, R30, R31, R32, R46, R47, R48, R49, R50, R51, R52, R53: 10k, Resistor_SMD:R_0603_1608Metric_Pad0.98x0.95mm_HandSolder
- removed TP3, TP4, TP8, TP9: TestPoint, Connector_Pin:Pin_D1.0mm_L10.0mm
- removed U9: TL074, Package_SO:TSSOP-14_4.4x5mm_P0.65mm
- removed kibuzzard-69A05110: G***, kibuzzard-69A05110
- removed kibuzzard-69A0514C: G***, kibuzzard-69A0514C
- removed kibuzzard-69A05154: G***, kibuzzard-69A05154
- added kibuzzard-69B01019: G***, kibuzzard-69B01019, F.Cu at (207.2, 84.4)
- added kibuzzard-69B01039: G***, kibuzzard-69B01039, F.Cu at (211.4, 106.2)
- added kibuzzard-69B01057: G***, kibuzzard-69B01057, F.Cu at (210.6, 84.4)
- C28, C32, C33, C34, C43, C44, C45, C46: value 330n -> 100n
- R14, R39: value 200k -> 100k
- R15, R40: value 100k -> 25k
- R16: value 22k -> 11k
- R17, R18, R19, R24, R42, R43, R44, R45: value 10k -> 100k
- R41: value 22k -> 100k
- R57: value 33k -> 47k
- moved R17 28.1 mm to (210.8, 81.8), turned to 0 degrees
- moved C43 27.4 mm to (211.3, 108.4)
- moved R18 23.9 mm to (210.8, 85.0), turned to 180 degrees
- moved C34 23.9 mm to (210.8, 83.4), turned to 0 degrees
- moved C44 23.4 mm to (211.3, 105.2)
- moved R45 23.4 mm to (211.3, 106.8)
- moved TP2 17.7 mm to (210.6, 89.4)
- moved TP5 17.2 mm to (211.4, 101.2), turned to -90 degrees
- moved C33 17.1 mm to (210.8, 86.6), turned to 0 degrees
- moved kibuzzard-69A0511F 16.4 mm to (208.0, 106.2)
- moved TP19 16.0 mm to (201.8, 97.4)
- moved kibuzzard-699DA06A 16.0 mm to (201.8, 101.6)
- moved R44 15.5 mm to (211.3, 103.6), turned to 0 degrees
- moved C45 15.1 mm to (207.4, 103.6)
- moved C46 14.6 mm to (207.4, 106.8)
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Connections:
- C32 pad 1: Net-(U7C-+) -> Net-(U7B-+)
- C44 pad 1: Net-(U9C-+) -> Net-(U7D-+)
- C45 pad 1: Net-(U9A-+) -> Net-(U7C-+)
- R19 pad 1: Net-(U7C-+) -> Net-(U7B-+)
- R43 pad 2: Net-(U9A-+) -> Net-(U7C-+)
- R44 pad 1: Net-(U9C-+) -> Net-(U7D-+)
- U1 pad 11: /Analog frontend/V_ADC_AC -> /Analog frontend/V_HighPass
- U1 pad 12: /Analog frontend/V_ADC_DC -> /Analog frontend/V_LowPass
- U1 pad 13: /Analog frontend/I_ADC_DC -> /Analog frontend/I_LowPass
- U1 pad 14: /Analog frontend/I_ADC_AC -> /Analog frontend/I_HighPass
- U10 pad 5: unconnected-(U10B-+-Pad5) -> GND
- U10 pad 6: unconnected-(U10B---Pad6) -> Net-(U10B--)
- U10 pad 7: unconnected-(U10-Pad7) -> Net-(U10B--)
- U12 pad 5: GND -> +1.65 V_{ref}
- U6 pad 5: GND -> +1.65 V_{ref}
- U7 pad 13: Net-(U7D--) -> /Analog frontend/I_HighPass
- U7 pad 14: /Analog frontend/V_ADC_AC -> /Analog frontend/I_HighPass
- U7 pad 6: Net-(U7B--) -> /Analog frontend/V_HighPass
- U7 pad 7: /Analog frontend/V_ADC_DC -> /Analog frontend/V_HighPass
- U7 pad 8: /Analog frontend/V_HighPass -> /Analog frontend/I_LowPass
- U7 pad 9: /Analog frontend/V_HighPass -> /Analog frontend/I_LowPass
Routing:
- net /Analog frontend/I_ADC_DC: track 84.8 -> 0.00 mm
- net /Analog frontend/V_ADC_DC: track 73.5 -> 0.00 mm
- net /Analog frontend/I_HighPass: track 8.12 -> 74.3 mm
- net /Analog frontend/V_ADC_AC: track 65.7 -> 0.00 mm
- net /Analog frontend/I_ADC_AC: track 65.2 -> 0.00 mm
- net /Analog frontend/I_LowPass: track 13.9 -> 76.7 mm, vias 0 -> 1
- net /Analog frontend/V_HighPass: track 9.37 -> 60.8 mm, vias 0 -> 1
- net /Analog frontend/V_LowPass: track 13.3 -> 61.2 mm, vias 0 -> 1
- net Net-(J7-In): track 58.9 -> 21.3 mm, vias 4 -> 0
- net Net-(C28-Pad2): track 58.3 -> 26.8 mm
- net SW_BYPASS_2_A: track 126.6 -> 97.3 mm, vias 5 -> 2
- net +1.65 V_{ref}: track 100.7 -> 76.4 mm, vias 5 -> 4
- net Net-(J8-In): track 49.8 -> 25.8 mm, vias 3 -> 1
- net Net-(J6-In): track 39.5 -> 18.0 mm, vias 4 -> 0
- net Net-(C43-Pad2): track 59.1 -> 42.1 mm
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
